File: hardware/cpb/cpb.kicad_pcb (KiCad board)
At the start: 6 copper layers, 95.9 x 90.2 mm, 239 parts, among them J1 Spacecraft Bus Stacking Conne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, J10 SW1, J11 SW2, J12 SW3, J13 PISW1, J14 μSW1, J15 μSW2, J16 μSW3, J17 μSW4, J2 I2CExt, J3 DAC1BUF, J4 DAC2BUF, J6 Raspberry Pi Zero 2W, J7 ADC6/7, J8 ADC2/3, J9 4FBRG, J99 RBFJUMP, Q1 PMBT2222A, Q10 BSS138PS,115, Q11 BSS138PS,115, Q12 MBT2222ADW1T1, Q13 MBT2222ADW1T1, Q14 BSS138PS,115, Q15 BSS138PS,115, Q16 MBT2222ADW1T1, Q17 MBT2222ADW1T1, Q18 BSS138PS,115, Q19 BSS138PS,115, Q2 IRF9393, Q20 MBT2222ADW1T1, Q21 MBT2222ADW1T1, Q22 BSS138PS,115, Q23 BSS138PS,115, Q24 MBT2222ADW1T1, Q25 IRF7306, Q26 MBT2222ADW1T1, Q27 IRF7306, Q28 MBT2222ADW1T1, Q29 IRF7306, Q3 MBT2222ADW1T1, Q30 MBT2222ADW1T1, Q31 IRF7306, Q4 PMBT2222A, Q5 PMBT2222A, Q6 IRF9393, Q7 PMBT2222A, Q8 MBT2222ADW1T1, Q9 MBT2222ADW1T1, U1 TS912, U2 ADR420ARMZ, U3 KF33BDT, U4 STM32L072R_B-Z_Tx, U5 AP62301WU, U6 SC16IS750xBS, U7 SC18IS606, U8 KF33BDT, U9 MAX22200, Y1 14.7456MHz

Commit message: hardware/cpb: further routing
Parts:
- turned R47 to 180 degrees
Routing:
- net /PISYNC: track 1.37 -> 66.5 mm, vias 1 -> 3
- net /ADC2: track 7.19 -> 37.3 mm, vias 4 -> 5
- net /ADC3: track 6.64 -> 35.4 mm, vias 4 -> 6
- net Net-(Q6-G): track 0.00 -> 6.56 mm
- net Net-(Q6-S-Pad1): track 0.00 -> 6.27 mm
- net Net-(Q9A-B1): track 4.92 -> 3.64 mm
- net /SDA: track 7.80 -> 8.92 mm
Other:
- board text added: "NyanSat Combined Payload Board Revision 1 E-006-001 2024; By TEV & MPL"
- board text removed: "NyanSat Combined Payload Board Revision 1 E-006-001 2024; By ___ & MPL"

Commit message: cpb: Continued work on layout
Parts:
- moved Q1 14.3 mm to (178.9, 140.4)
- moved C5 6.23 mm to (166.2, 132.7)
- moved J3 6.20 mm to (113.6, 140.7)
- moved J4 5.80 mm to (119.8, 140.7)
- moved L1 0.80 mm to (145.0, 134.3)
- turned R22 to -90 degrees
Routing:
- net /PRIPWREN: track 0.00 -> 105.3 mm, vias 1 -> 2
- net /DAC2FB: track 1.46 -> 62.5 mm, vias 3 -> 5
- net /SDA: track 8.92 -> 61.6 mm
- net /uTX: track 1.57 -> 51.7 mm, vias 2 -> 5
- net /uRX: track 1.60 -> 47.1 mm, vias 2 -> 5
- net /SCL: track 6.34 -> 50.4 mm
- net /EN5V: track 0.81 -> 39.4 mm, vias 3 -> 5
- net /PILED: track 0.83 -> 39.3 mm, vias 1 -> 2
- net /TIM3_CH2: track 2.06 -> 39.0 mm
- net /PIFAILSAFE: track 0.94 -> 36.0 mm, vias 1 -> 2
- net /FBRGPWREN: track 0.00 -> 33.5 mm, vias 1 -> 2
- net /SW3: track 1.49 -> 34.8 mm, vias 2 -> 3
- net /PI3V3: track 1.57 -> 34.8 mm, vias 2 -> 3
- net /~{PIRTS}: track 0.94 -> 33.2 mm, vias 1 -> 2
- net Net-(U6-~{RESET}): track 0.74 -> 32.6 mm, vias 2 -> 3
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
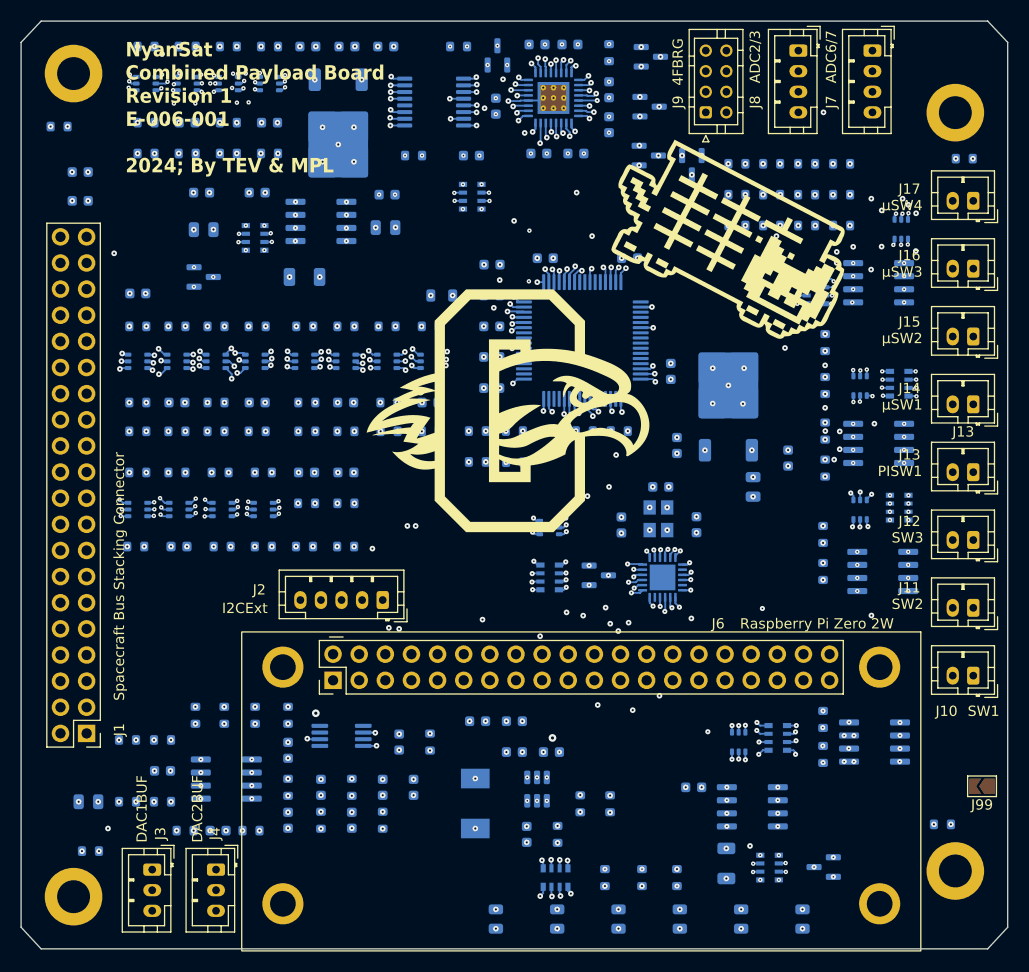
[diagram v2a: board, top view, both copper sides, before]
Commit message: cpb: route a few more traces; 103 remain
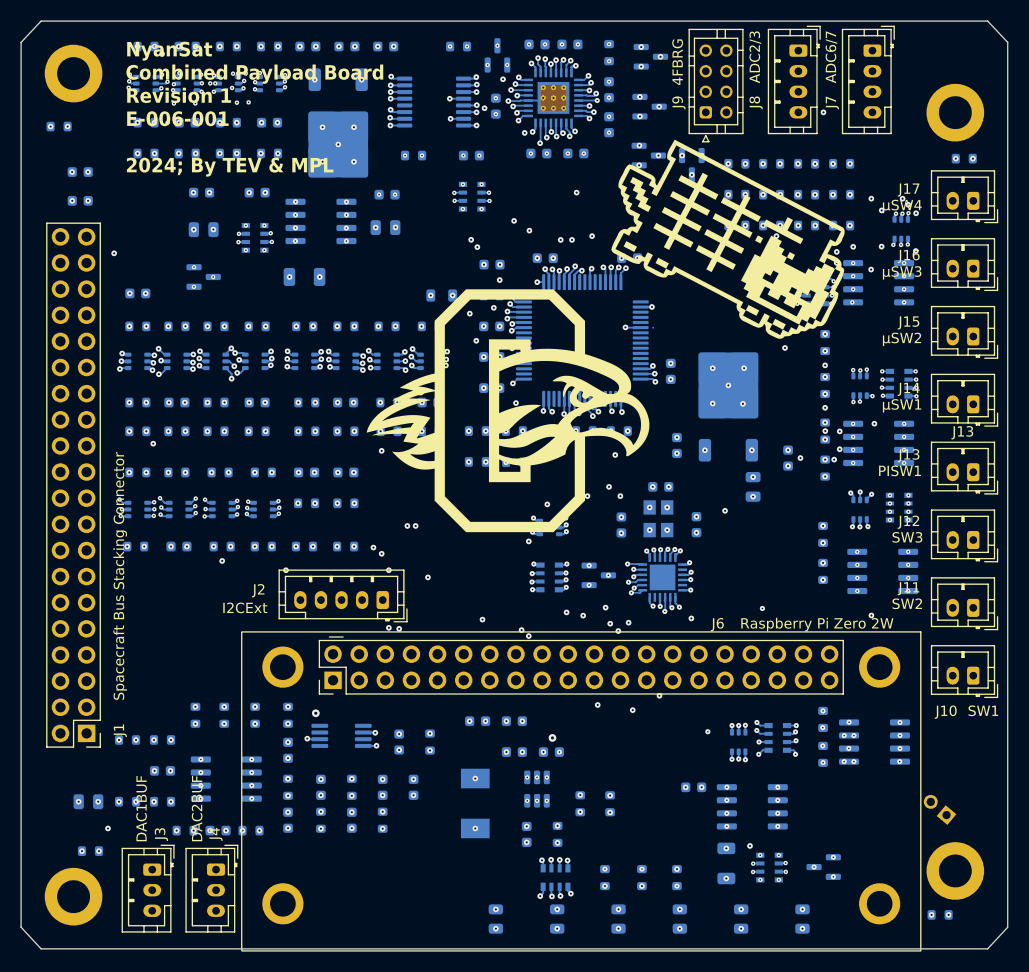
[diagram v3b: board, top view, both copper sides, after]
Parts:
- J99: footprint Jumper:SolderJumper-2_P1.3mm_Open_TrianglePad1.0x1.5mm -> Connector_PinHeader_2.00mm:PinHeader_1x02_P2.00mm_Horizontal; moved to B.Cu
- moved R40 8.80 mm to (190.2, 145.1)
- moved J99 4.44 mm to (190.8, 135.4), turned to 50 degrees
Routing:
- net /DAC1: track 1.11 -> 75.7 mm, vias 2 -> 6
- net /~{RBF}: track 4.99 -> 78.3 mm, vias 3 -> 4
- net /DAC2: track 1.49 -> 73.8 mm, vias 2 -> 4
- net /UARTSCL: track 2.20 -> 73.0 mm, vias 5 -> 8
- net /DAC1FB: track 3.38 -> 72.0 mm, vias 3 -> 5
- net /UARTSDA: track 2.92 -> 68.0 mm, vias 5 -> 6
- net /SWDIO: track 1.31 -> 41.1 mm, vias 1 -> 2
- net /~{MICRORST}: track 5.29 -> 36.1 mm
- net /SWCLK: track 1.32 -> 31.8 mm, vias 1 -> 3
- net /PISW1: track 0.00 -> 30.0 mm, vias 1 -> 2
- net /TIM3_CH2: track 39.0 -> 61.6 mm
- net /RSTREQGPIO: track 5.61 -> 26.0 mm, vias 3 -> 4
- net Net-(J6-Pin_22): track 6.53 -> 25.4 mm
- net Net-(U4-PC3): track 31.3 -> 45.7 mm, vias 2 -> 3
- net /~{RSTREQPI}: track 8.39 -> 20.6 mm, vias 2 -> 3
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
